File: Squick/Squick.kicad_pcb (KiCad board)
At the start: 2 copper layers, 99 parts, among them J1 BT, J10 D24V3F-5V, J2 DEBUG_UART, J3 PROG, J4 VL53L0X_L, J5 VL53L0X_F, J6 VL53L0X_R, J7 ENK_L, J8 ENK_R, J9 BATT, SW1 USER_BUT_1, SW2 USER_BUT_2, SW3 RESET, SW4 ON/OFF, T1 SFH-313FA, T2 SFH-313FA, T3 SFH-313FA, T4 SFH-313FA, T5 SFH-313FA, T6 SFH-313FA, U1 STM32F411RETx, U10 LM1117-3.3, U2 CD4051B, U3 KTIR0711S, U4 CD4051B, U5 KTIR0711S, U6 KTIR0711S, U7 KTIR0711S, U8 Adafruit_4634, U9 TB6612FNG

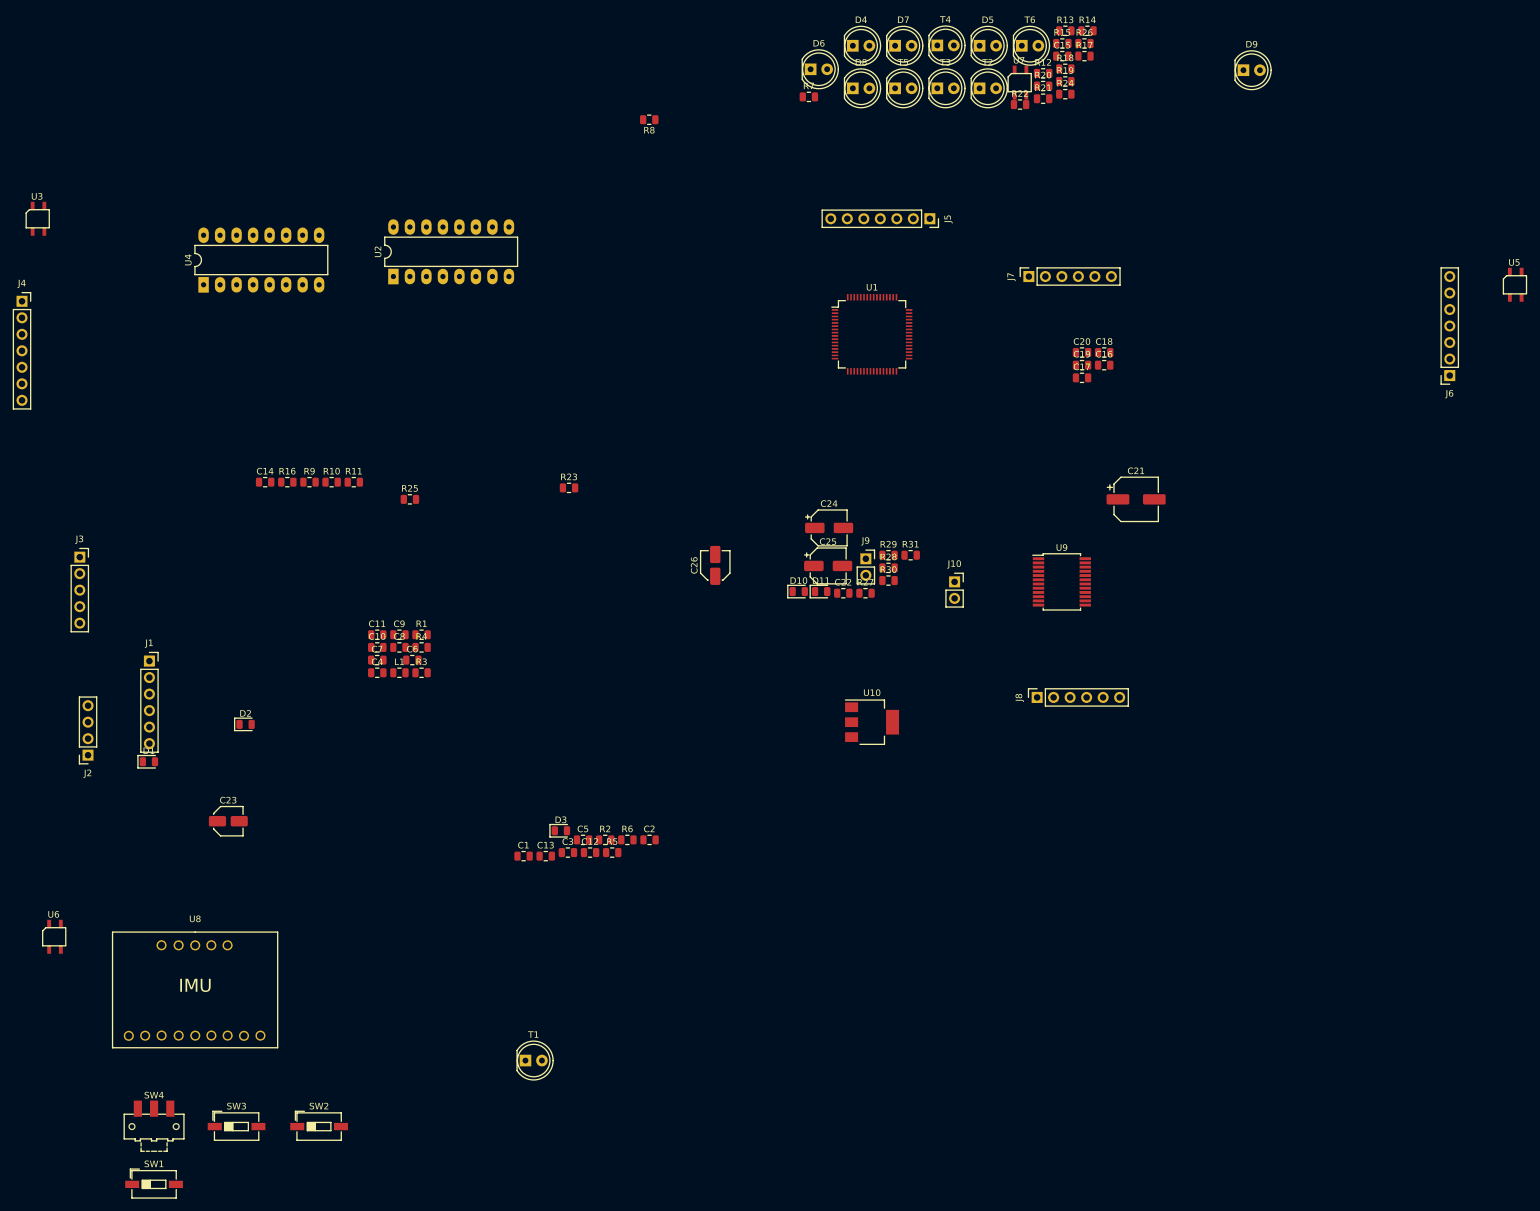
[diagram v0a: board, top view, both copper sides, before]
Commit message: Progress with PCB and some footprint debugs
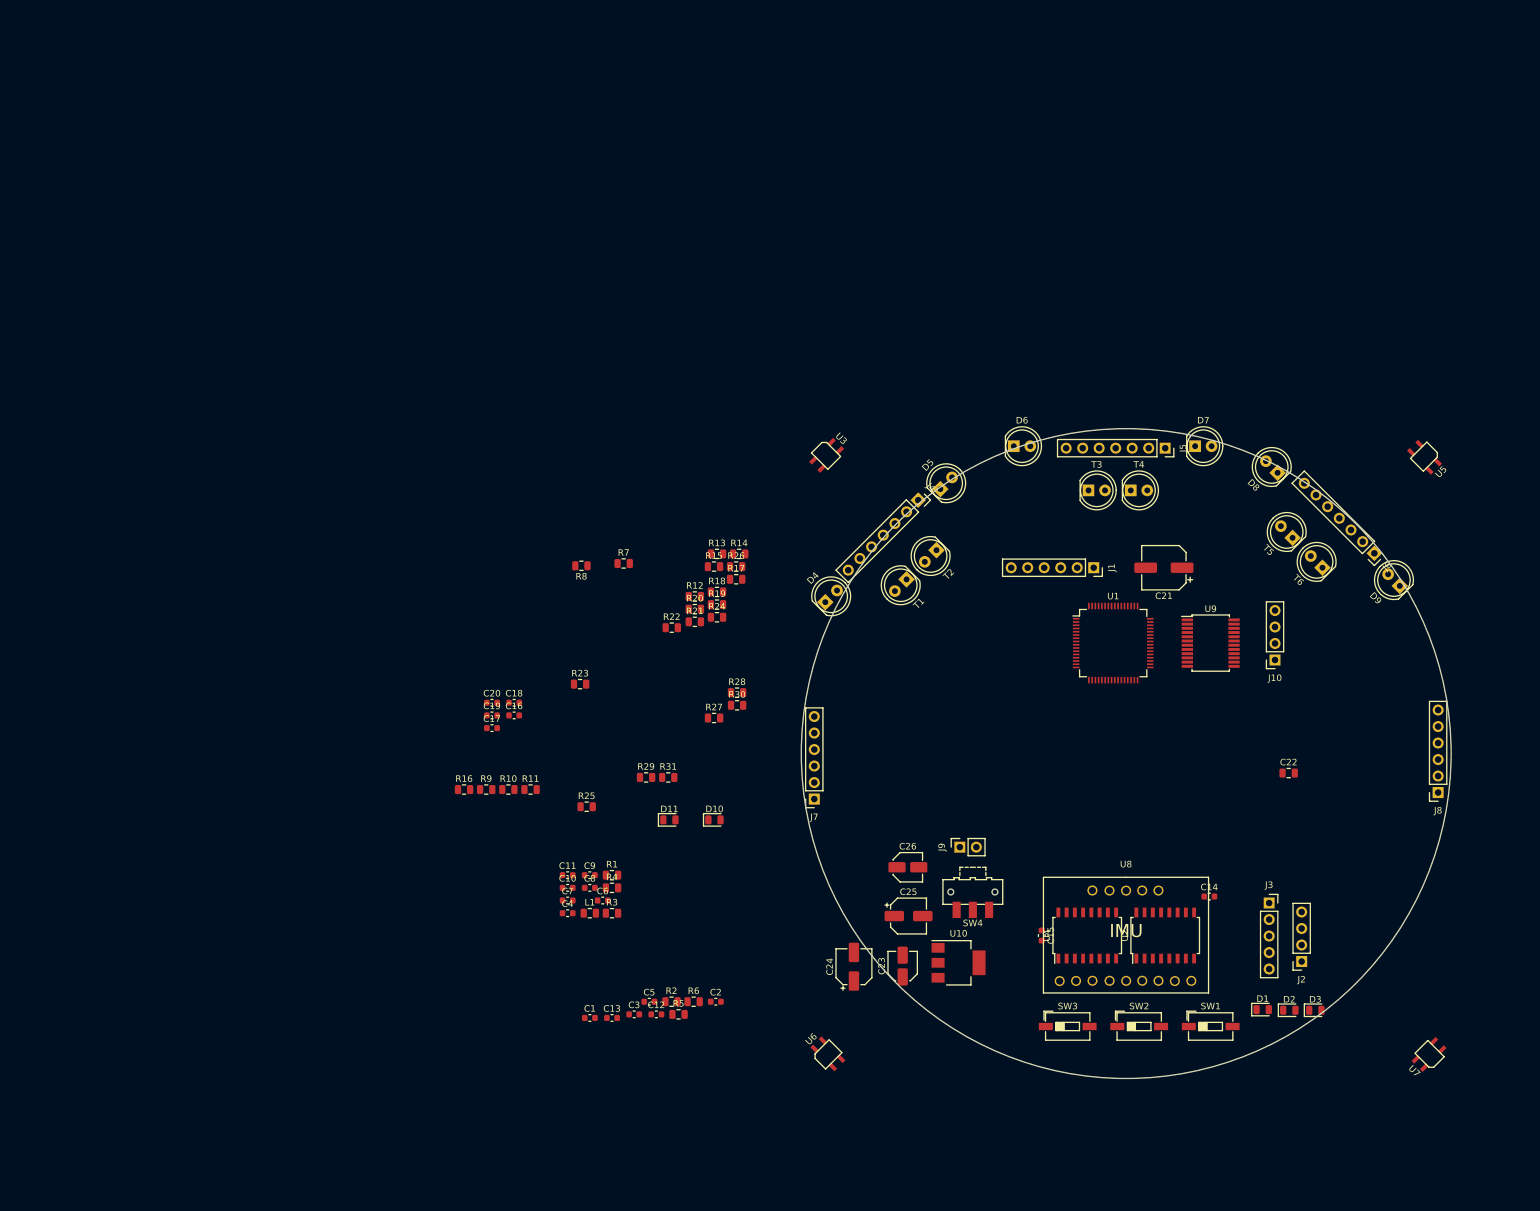
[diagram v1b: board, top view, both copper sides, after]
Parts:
- C1, C10, C11, C12, C13, C14, C15, C16, C17, C18, C19, C2, C20, C3, C4, C5, C6, C7, C8, C9: footprint Capacitor_SMD:C_0805_2012Metric -> Capacitor_SMD:C_0603_1608Metric
- J10: footprint Connector_PinSocket_2.54mm:PinSocket_1x02_P2.54mm_Vertical -> Connector_PinSocket_2.54mm:PinSocket_1x04_P2.54mm_Vertical
- U2, U4: footprint Package_DIP:DIP-16_W7.62mm_LongPads -> Package_SO:SOIC-16W_5.3x10.2mm_P1.27mm
- moved J3 190.6 mm to (197.0, 118.0)
- moved J2 189.4 mm to (202.0, 127.0)
- moved D1 175.6 mm to (196.0, 134.4)
- moved U4 168.9 mm to (169.0, 123.0)
- moved D2 166.5 mm to (200.1, 134.5)
- moved SW1 164.4 mm to (188.0, 137.0)
- moved U7 162.2 mm to (221.6, 141.3), turned to 135 degrees
- moved C14 158.7 mm to (187.8, 117.0)
- moved U2 156.2 mm to (181.0, 123.0)
- moved J1 146.0 mm to (170.0, 66.4), turned to 270 degrees
- moved U8 143.5 mm to (175.0, 130.0)
- moved J4 141.3 mm to (143.0, 56.0), turned to 315 degrees
- moved C15 135.4 mm to (162.0, 123.0), turned to 270 degrees
- moved SW4 131.1 mm to (151.4, 116.3), turned to 180 degrees
- moved SW3 128.8 mm to (166.0, 137.0)
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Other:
- board outline added: 100 x 100 mm

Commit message: Progress with PCB and size reducement
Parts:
- C14, C15, C22, R12, R13, R14, R15, R17, R18, R19, R20, R21, R22, R24, R26, U3, U5, U6, U7: moved to B.Cu
- moved R13 89.8 mm to (192.6, 103.9)
- moved R14 89.8 mm to (196.0, 103.9)
- moved R15 88.2 mm to (192.2, 102.0)
- moved R26 88.2 mm to (195.6, 102.0)
- moved R17 86.7 mm to (195.6, 100.0)
- moved R18 85.3 mm to (192.6, 98.1)
- moved R12 84.8 mm to (189.2, 97.4)
- moved R19 84.1 mm to (192.6, 96.1)
- moved R20 83.7 mm to (189.2, 95.4)
- moved R24 83.1 mm to (192.6, 94.2)
- moved R21 82.7 mm to (189.2, 93.5)
- moved R22 82.3 mm to (185.7, 92.6)
- moved SW4 69.3 mm to (209.8, 79.0), turned to 90 degrees
- moved SW1 62.8 mm to (153.5, 84.5)
- moved SW2 62.1 mm to (143.6, 84.6)
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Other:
- board size 100 x 100 mm -> 80 x 80 mm

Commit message: Major progress with PCB design
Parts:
- C22: moved to F.Cu
- C23, C26: footprint Capacitor_SMD:C_Elec_4x5.4 -> Capacitor_SMD:C_0603_1608Metric
- D10, D11, R25, R29, R31, U1: moved to B.Cu
- moved R25 106.7 mm to (195.6, 77.5)
- moved D11 98.3 mm to (200.1, 81.5)
- moved R31 97.9 mm to (200.1, 77.5)
- moved R29 96.1 mm to (195.7, 81.5)
- moved D10 93.8 mm to (199.9, 73.5)
- moved C22 92.7 mm to (118.0, 73.4)
- moved SW4 68.6 mm to (154.3, 119.4), turned to 315 degrees
- moved J10 60.1 mm to (139.1, 98.9)
- moved J9 58.8 mm to (162.6, 123.9), turned to 90 degrees
- moved C15 54.8 mm to (172.8, 58.0)
- moved U4 54.8 mm to (172.7, 58.0)
- moved SW1 54.6 mm to (204.6, 65.0), turned to 135 degrees
- moved U2 54.1 mm to (185.1, 58.0)
- moved C14 54.0 mm to (184.2, 58.0)
- moved U8 53.8 mm to (179.2, 65.4)
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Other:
- board size 80 x 80 mm -> 92 x 92 mm

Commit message: PCB project almost finished (without connections)
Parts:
- added Q1: Q_PMOS_GSD, Package_TO_SOT_SMD:SOT-23, F.Cu at (150.6, 109.0)
- C1, C13, C2, C8, R16, R23, R4: moved to B.Cu
- D10, D11, R12, R17, R25, R29, R31: moved to F.Cu
- R28: value 1.5k -> 10k
- SW4: value ON/OFF -> SW_SPDT
- moved R23 122.8 mm to (208.8, 119.0), turned to 135 degrees
- moved R16 121.8 mm to (218.8, 49.3), turned to 225 degrees
- moved R4 105.5 mm to (201.4, 116.2), turned to 270 degrees
- moved C4 98.4 mm to (186.9, 109.4), turned to 270 degrees
- moved L1 97.1 mm to (187.9, 101.8)
- moved C8 96.9 mm to (188.9, 106.4), turned to 180 degrees
- moved R1 96.4 mm to (192.2, 117.2)
- moved C7 96.4 mm to (185.1, 109.4), turned to 90 degrees
- moved C10 94.3 mm to (183.1, 109.5), turned to 90 degrees
- moved R3 92.3 mm to (188.1, 120.4), turned to 180 degrees
- moved C13 92.1 mm to (201.2, 96.4)
- moved C11 92.1 mm to (181.0, 109.4), turned to 270 degrees
- moved R11 86.3 mm to (191.7, 48.2), turned to 180 degrees
- moved C6 85.0 mm to (179.0, 109.4), turned to 270 degrees
- moved R10 84.8 mm to (187.1, 49.2), turned to 270 degrees
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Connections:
- R28 pad 1: GND -> Net-(Q1-Pad1)
- R28 pad 2: Net-(Q1-Pad1) -> GND

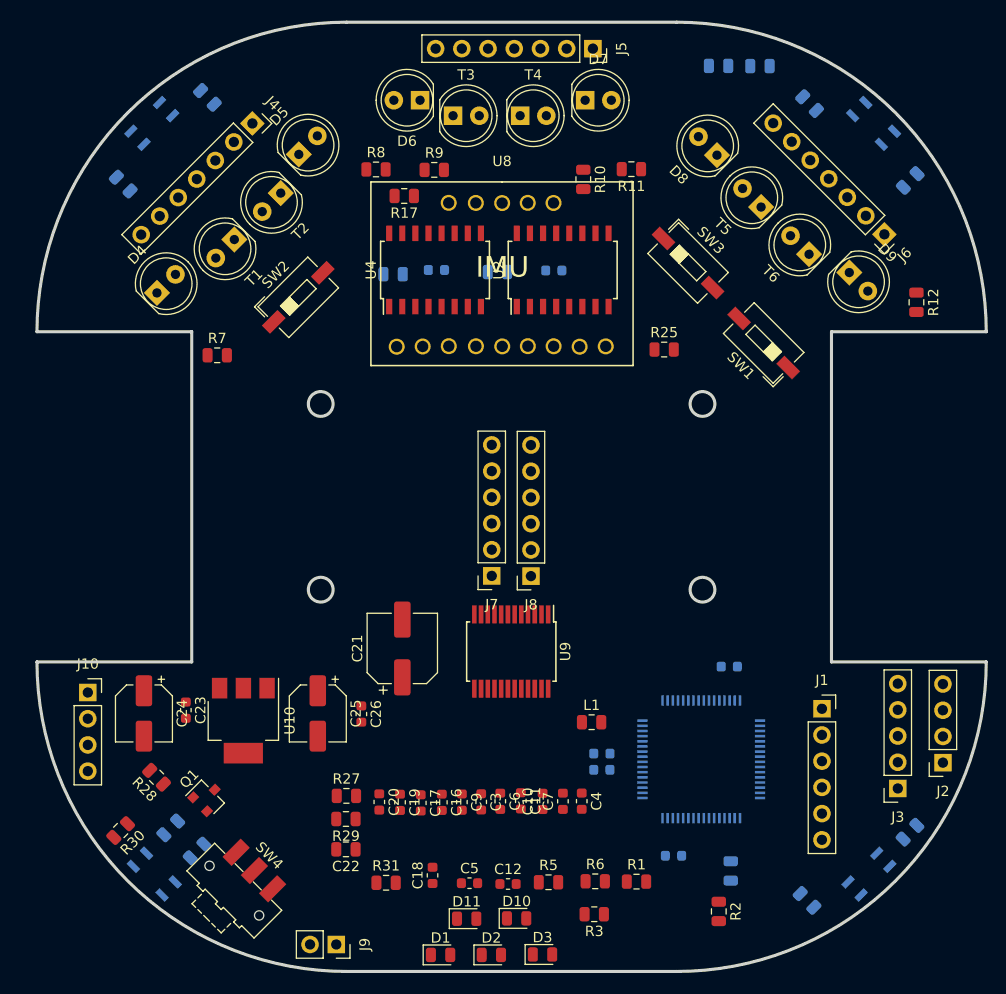
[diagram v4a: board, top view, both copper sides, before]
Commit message: Changed IMU and assigned 0603 footprints
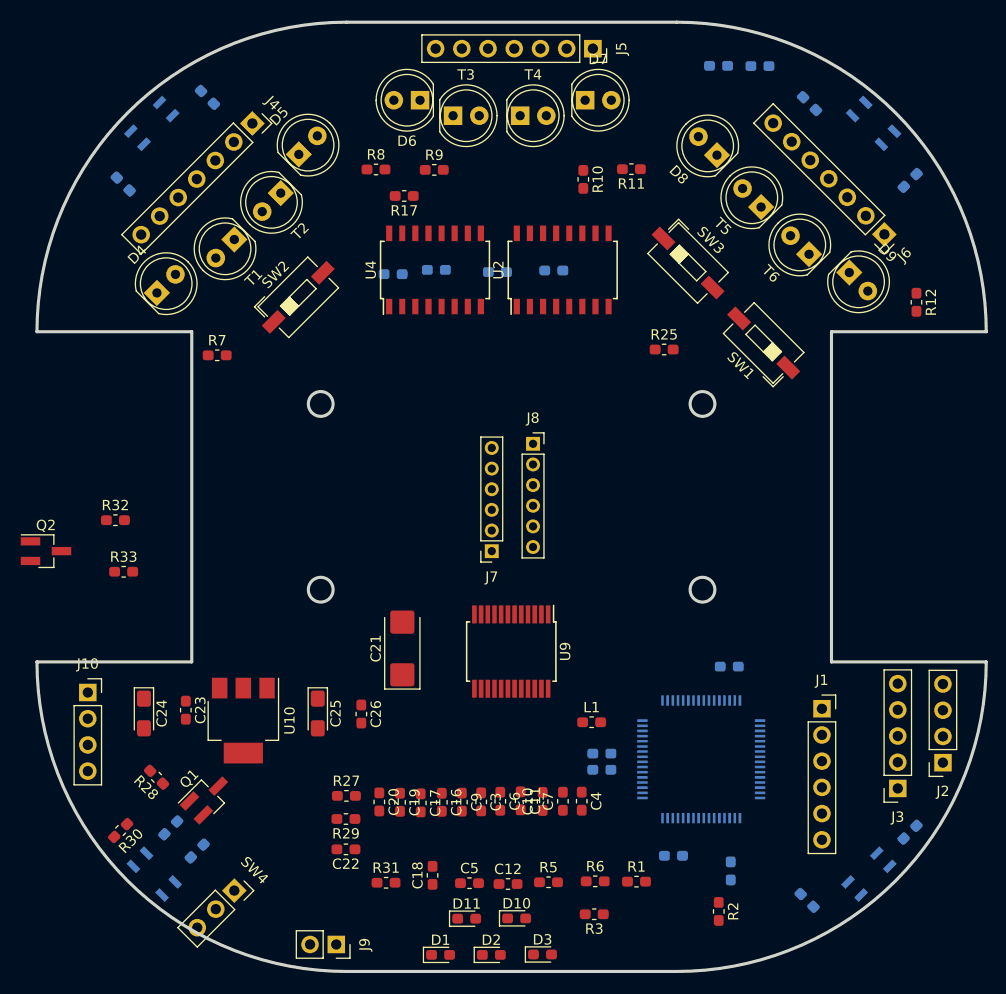
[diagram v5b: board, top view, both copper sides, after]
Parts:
- removed U8: Adafruit_4634, Symbol:IMU_LSM9DS1_Adafruit4634
- added Q2: AO3407A, Package_TO_SOT_SMD:SOT-23_Handsoldering, F.Cu at (135.0, 85.2)
- added R32: 10k, Resistor_SMD:R_0603_1608Metric_Pad1.05x0.95mm_HandSolder, F.Cu at (141.7, 82.2)
- added R33: 1k, Resistor_SMD:R_0603_1608Metric_Pad1.05x0.95mm_HandSolder, F.Cu at (142.5, 87.2)
- C1, C10, C11, C12, C13, C14, C15, C16, C17, C18, C19, C2, C20, C23, C26, C3, C4, C5, C6, C7, C8, C9: footprint Capacitor_SMD:C_0603_1608Metric -> Capacitor_SMD:C_0603_1608Metric_Pad1.05x0.95mm_HandSolder
- C21: footprint Capacitor_SMD:CP_Elec_6.3x5.9 -> Capacitor_Tantalum_SMD:CP_EIA-6032-28_Kemet-C_Pad2.25x2.35mm_HandSolder
- C22: footprint Capacitor_SMD:C_0805_2012Metric -> Capacitor_SMD:C_0603_1608Metric_Pad1.05x0.95mm_HandSolder
- C24, C25: footprint Capacitor_SMD:CP_Elec_5x5.4 -> Capacitor_Tantalum_SMD:CP_EIA-3216-18_Kemet-A_Pad1.58x1.35mm_HandSolder
- D1, D10, D11, D2, D3: footprint LED_SMD:LED_0805_2012Metric -> LED_SMD:LED_0603_1608Metric_Pad1.05x0.95mm_HandSolder
- J7, J8: footprint Connector_PinSocket_2.54mm:PinSocket_1x06_P2.54mm_Vertical -> Connector_PinSocket_2.00mm:PinSocket_1x06_P2.00mm_Vertical
- L1: footprint Inductor_SMD:L_0805_2012Metric -> Inductor_SMD:L_0603_1608Metric_Pad1.05x0.95mm_HandSolder
- Q1: value Q_PMOS_GSD -> AO3407A; footprint Package_TO_SOT_SMD:SOT-23 -> Package_TO_SOT_SMD:SOT-23_Handsoldering
- R1, R10, R11, R12, R13, R14, R15, R16, R18, R19, R2, R21, R23, R27, R29, R3, R30, R31, R4, R5, R6, R7, R8, R9: footprint Resistor_SMD:R_0805_2012Metric -> Resistor_SMD:R_0603_1608Metric_Pad1.05x0.95mm_HandSolder
- R17, R20, R22, R24, R25, R26: value 200 -> 220; footprint Resistor_SMD:R_0805_2012Metric -> Resistor_SMD:R_0603_1608Metric_Pad1.05x0.95mm_HandSolder
- R28: value 10k -> 1k; footprint Resistor_SMD:R_0805_2012Metric -> Resistor_SMD:R_0603_1608Metric_Pad1.05x0.95mm_HandSolder
- SW4: value SW_SPDT -> ON/OFF; footprint Button_Switch_SMD:SW_SPDT_CK-JS102011SAQN -> Connector_PinSocket_2.54mm:PinSocket_1x03_P2.54mm_Vertical
- moved J8 12.8 mm to (182.2, 74.8), turned to 0 degrees
- moved J7 2.40 mm to (178.2, 85.2)
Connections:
- Q1 pad 2: Vin -> Net-(Q1-Pad2)
- Q1 pad 3: Net-(Q1-Pad3) -> VCC
- SW4 pad 1: VCC -> GND
- SW4 pad 2: Net-(Q1-Pad3) -> Net-(R33-Pad2)
- SW4 pad 3: Net-(Q1-Pad3) -> Net-(R33-Pad2)
- U9 pad 1: M1_L -> M1_R
- U9 pad 11: M1_R -> M1_L
- U9 pad 12: M1_R -> M1_L
- U9 pad 15: PWM_R -> PWM_L
- U9 pad 16: R_IN2 -> L_IN2
- U9 pad 17: R_IN1 -> L_IN1
- U9 pad 2: M1_L -> M1_R
- U9 pad 21: L_IN1 -> R_IN1
- U9 pad 22: L_IN2 -> R_IN2
- U9 pad 23: PWM_L -> PWM_R
- U9 pad 5: M2_L -> M2_R
- U9 pad 6: M2_L -> M2_R
- U9 pad 7: M2_R -> M2_L
- U9 pad 8: M2_R -> M2_L

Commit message: some debugs and small changes
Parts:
- added U8: Adafruit_4554, IMU_Adafruit-4554:IMU_LSM9DS1_Adafruit4634, F.Cu at (189.8, 50.8)
- C10, C11, C12, C16, C17, C18, C19, C20, C22, C3, C4, C5, C6, C7, C9, R1, R27, R29, R5, R6: moved to B.Cu
- R24, R4: moved to F.Cu
- moved C15 53.9 mm to (162.1, 110.7), turned to 270 degrees
- moved C14 53.0 mm to (181.4, 110.9), turned to 270 degrees
- moved R30 44.7 mm to (186.4, 119.7), turned to 0 degrees
- moved R20 39.4 mm to (139.8, 52.2), turned to 135 degrees
- moved R32 33.7 mm to (151.4, 114.4), turned to 315 degrees
- moved R1 33.6 mm to (158.7, 118.5), turned to 180 degrees
- moved R33 33.4 mm to (151.8, 119.3)
- moved R2 31.3 mm to (168.9, 119.7), turned to 180 degrees
- moved Q2 29.1 mm to (150.0, 110.2), turned to 45 degrees
- moved R6 25.6 mm to (162.7, 118.5), turned to 180 degrees
- moved C22 25.4 mm to (189.4, 115.3), turned to 0 degrees
- moved R29 25.4 mm to (189.4, 112.3), turned to 0 degrees
- moved R27 25.2 mm to (189.3, 110.2), turned to 180 degrees
- moved R4 25.0 mm to (176.6, 119.8), turned to 180 degrees
- moved C4 23.0 mm to (164.0, 110.7)
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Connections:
- net IMU_DRDY renamed Net-(U1-Pad24)
- net IMU_INT1 renamed Net-(U1-Pad26)
- net IMU_INTM renamed Net-(U1-Pad25)
- net IMU_M renamed Net-(U1-Pad33)
- U1 pad 22: MISO -> Net-(U1-Pad22)
- U1 pad 23: MOSI -> Net-(U1-Pad23)
- U1 pad 27: IMU_INT2 -> LED_3
- U1 pad 28: DEN -> LED_2
- U1 pad 29: IMU_AG -> LED_1
- U1 pad 51: LED_3 -> BT_EN
- U1 pad 52: LED_2 -> BT_State
- U1 pad 53: LED_1 -> IMU_CS
- U1 pad 54: Net-(U1-Pad54) -> IMU_INT
- U1 pad 56: BT_EN -> MISO
- U1 pad 57: BT_State -> MOSI
